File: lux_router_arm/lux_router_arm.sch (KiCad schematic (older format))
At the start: 18 parts

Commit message: Most of the lux router
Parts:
- removed F? (x8): FUSE, symbol FUSE
- removed P? (x8): CONN_4, symbol CONN_4
- removed U?: SN65HVD09, MODULE, symbol SN65HVD09
- removed U?: TM4C1232D5PM, MODULE, symbol TM4C1232D5PM
- added C? (x2): C, symbol C
- added CONN?: AURORA_CARD, MODULE, symbol AURORA_CARD
- added D? (x2): ZENER 3V3, symbol ZENER
- added R? (x2): 100, symbol R
- added U?: TM4C1231D5PM, MODULE, symbol TM4C1231D5PM
- added X?: CRYSTAL, symbol CRYSTAL
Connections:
- net labels added: +3.3V, +5V, RTS0, RTS1, RTS2, RTS3, RTS4, RTS5, RTS6, RTS7, RX0, RX1, RX1_L, RX2, RX3, RX4, RX5, RX6, RX6_L, RX7, TX0, TX1, TX2, TX3, TX4, TX5, TX6, TX7
- net labels removed: VCC, VDD
- wire segments 105 -> 92
- no-connect marks 0 -> 5

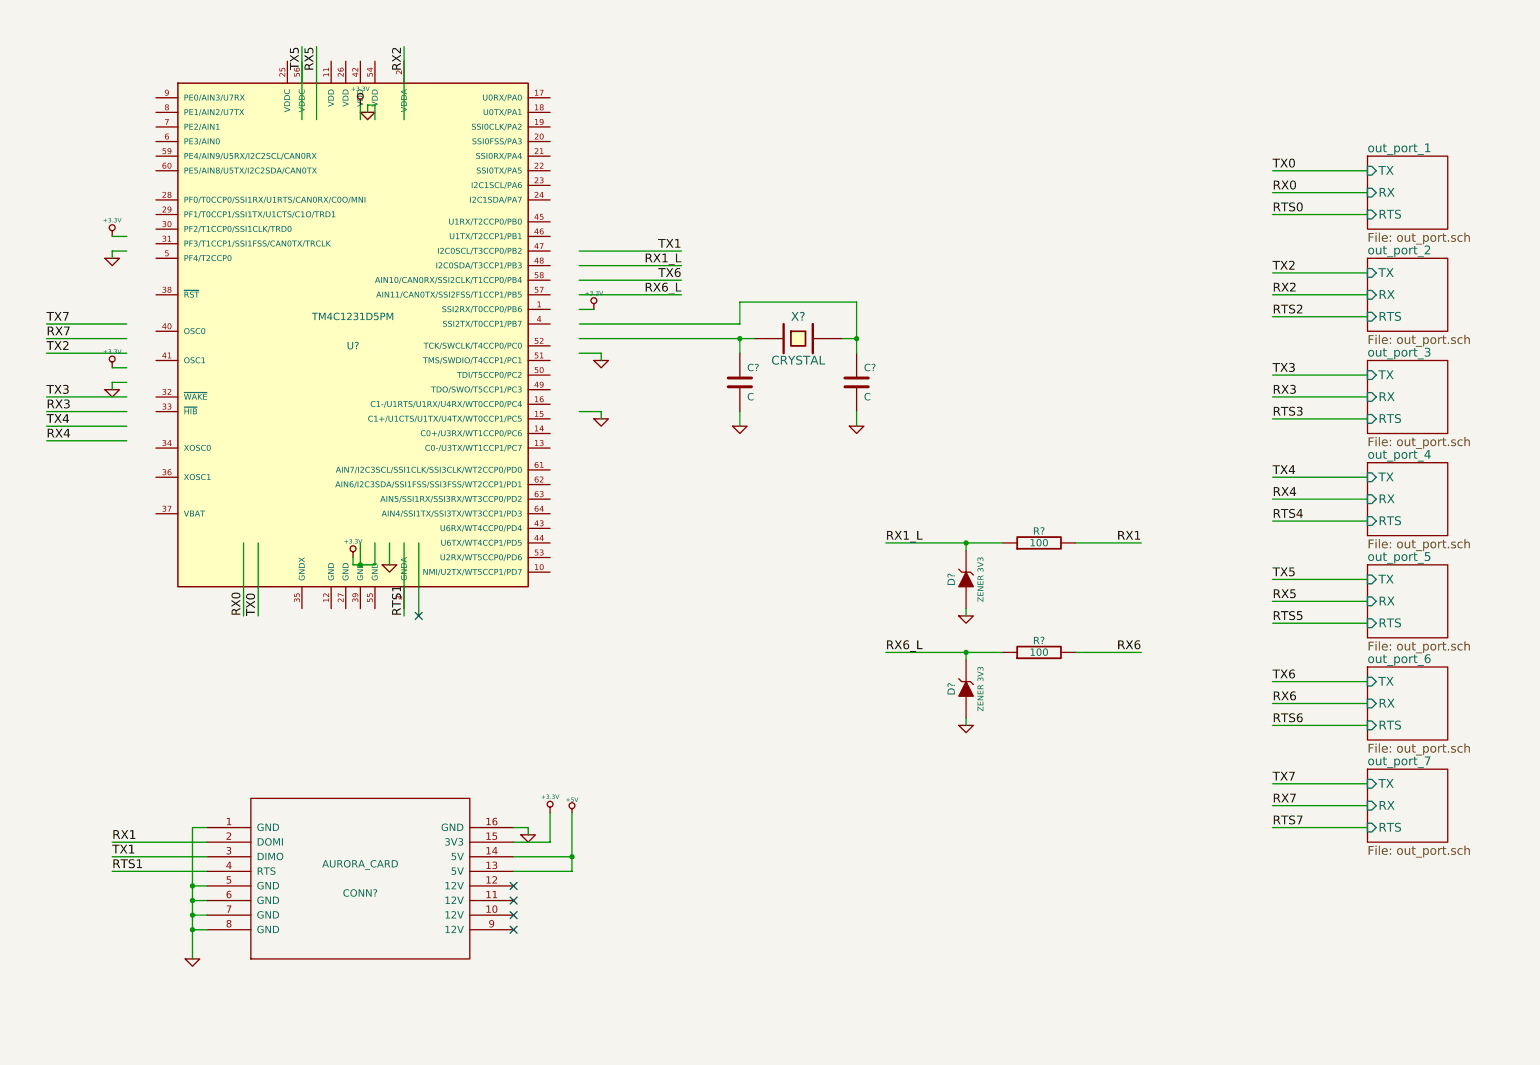
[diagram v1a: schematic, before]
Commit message: Prelimary parts assignment to lux router
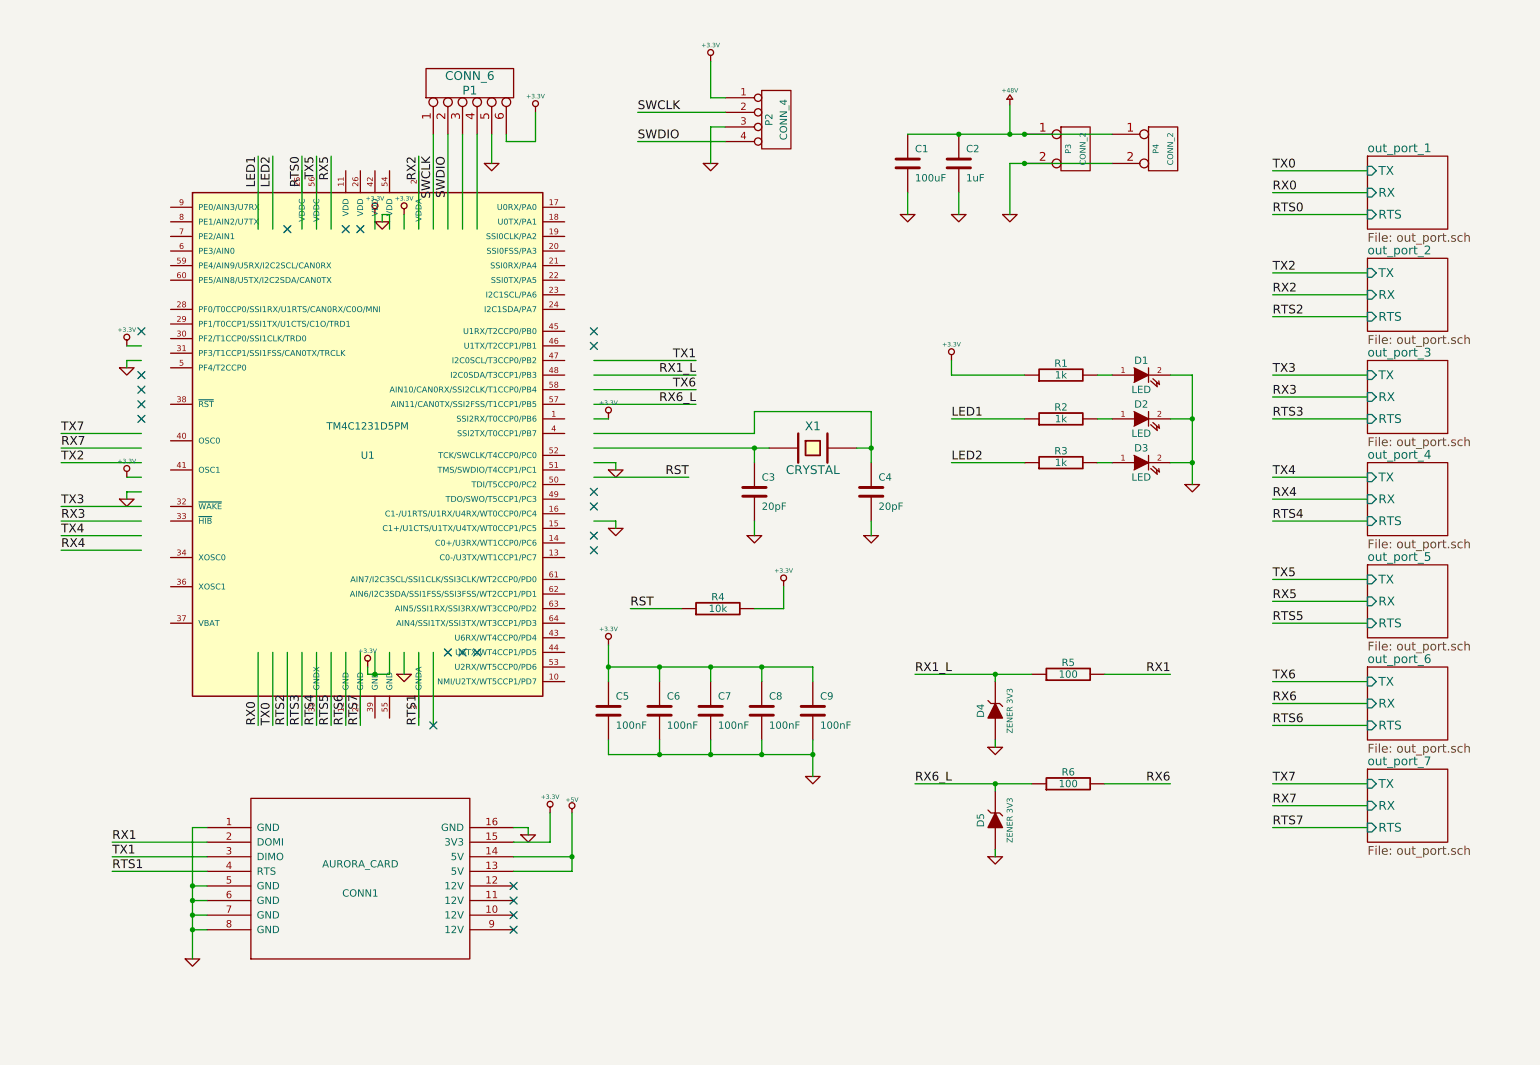
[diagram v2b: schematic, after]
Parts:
- added C1: 100uF, symbol C
- added C2: 1uF, symbol C
- added C5, C6, C7, C8, C9: 100nF, symbol C
- added D1, D2, D3: LED, symbol LED
- added P1: CONN_6, symbol CONN_6
- added P2: CONN_4, symbol CONN_4
- added P3, P4: CONN_2, symbol CONN_2
- added R1, R2, R3: 1k, symbol R
- added R4: 10k, symbol R
- C3, C4: renamed from C?; value C -> 20pF
- gave numbers to parts that had none: 7
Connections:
- net labels added: +48V, LED1, LED2, RST, SWCLK, SWDIO
- wire segments 92 -> 149
- no-connect marks 5 -> 22
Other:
- moved on the sheet: C3, C4, D4, D5, R5, R6, U1, X1

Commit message: Routed & ordered lux router board
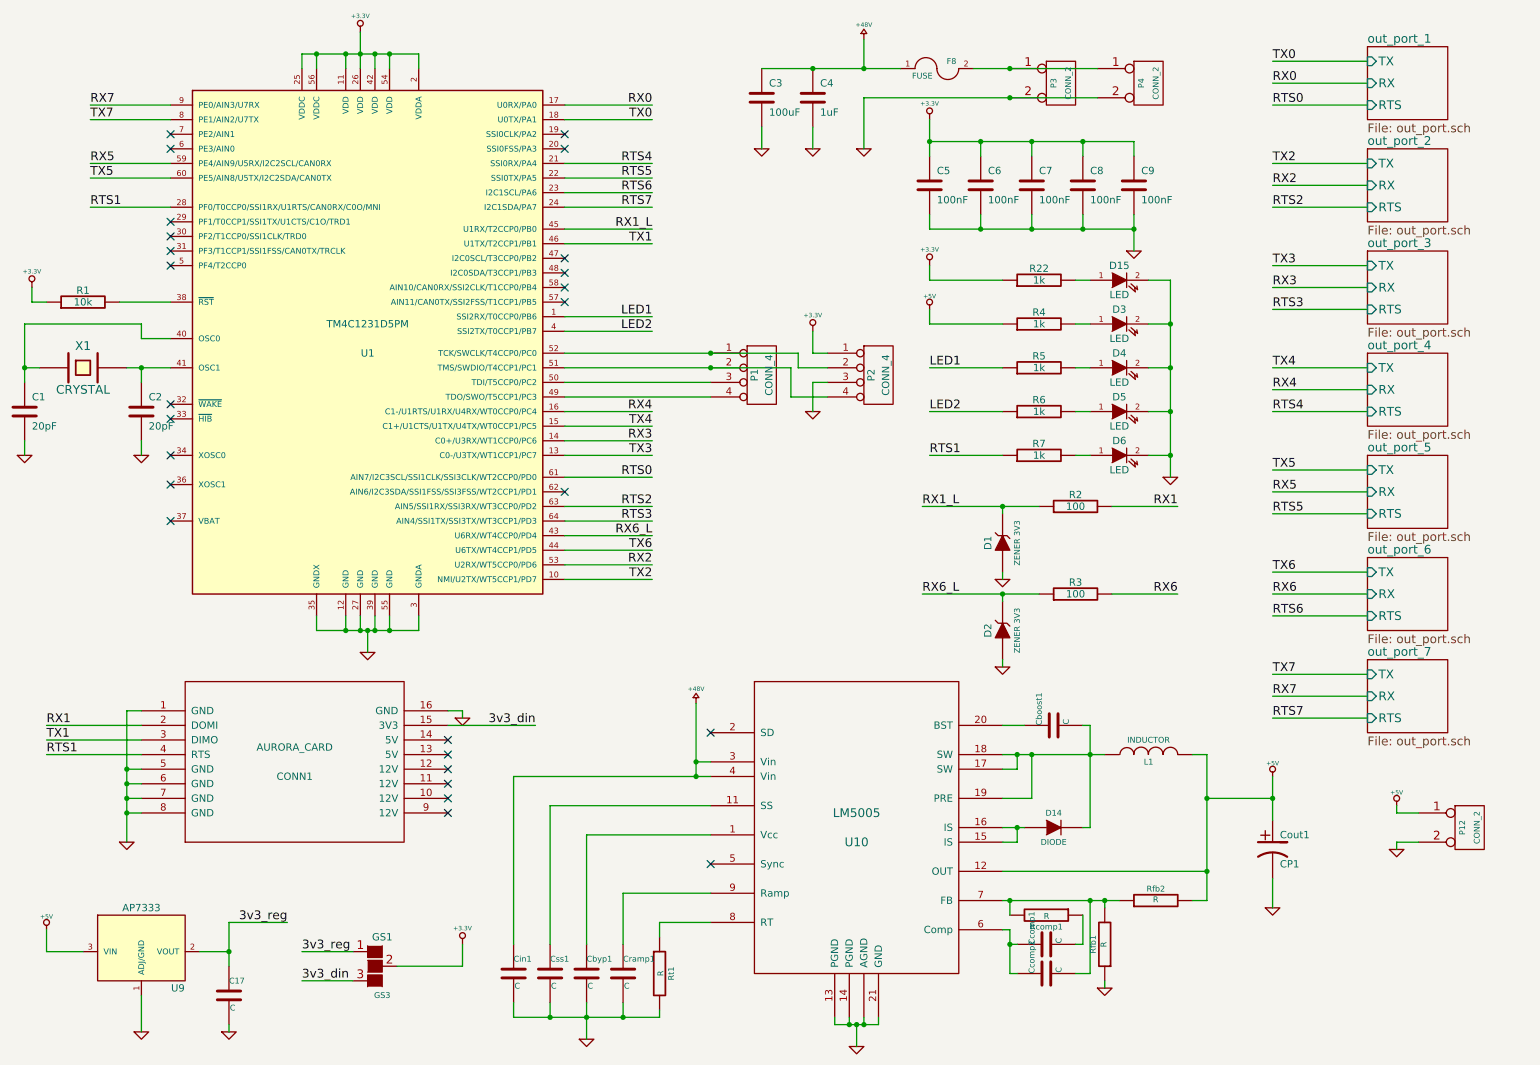
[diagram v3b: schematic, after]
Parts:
- removed P1: CONN_6, symbol CONN_6
- added C17, Cboost1, Cbyp1, Ccomp1, Ccomp2, Cin1, Cramp1, Css1: C, symbol C
- added Cout1: CP1, symbol CP1
- added D14: DIODE, symbol DIODE
- added D15, D6: LED, symbol LED
- added F8: FUSE, symbol FUSE
- added GS1: GS3, symbol GS3
- added L1: INDUCTOR, symbol INDUCTOR
- added P1: CONN_4, symbol CONN_4
- added P12: CONN_2, symbol CONN_2
- added R22, R7: 1k, symbol R
- added Rcomp1, Rfb1, Rfb2, Rt1: R, symbol R
- added U10: LM5005, symbol LM5005
- added U9: AP7333, symbol AP1117
- renumbered C3 to C1, C4 to C2, C1 to C3, C2 to C4, D4 to D1, D5 to D2, D1 to D3, D2 to D4, D3 to D5, R4 to R1, R5 to R2, R6 to R3, R1 to R4, R2 to R5, R3 to R6
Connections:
- net labels added: 3v3_din, 3v3_reg
- net labels removed: RST, SWCLK, SWDIO
- wire segments 149 -> 273
- no-connect marks 22 -> 26
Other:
- moved on the sheet: C1, C2, C3, C4, C5, C6, C7, C8, C9, CONN1, D1, D2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
